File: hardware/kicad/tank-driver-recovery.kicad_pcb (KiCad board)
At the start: 2 copper layers, 170 x 110 mm, 15 parts, among them P101 JTR-PRI, P102 JTR-SEC, P103 JTR-PWR, Q101 BD139-16, Q102 BD140-16, Q103 BD139-16, Q104 BD140-16, U101 OPA1656IDR, U102 OPA1656IDR, U103 OPA1656IDR, U104 OPA1656IDR

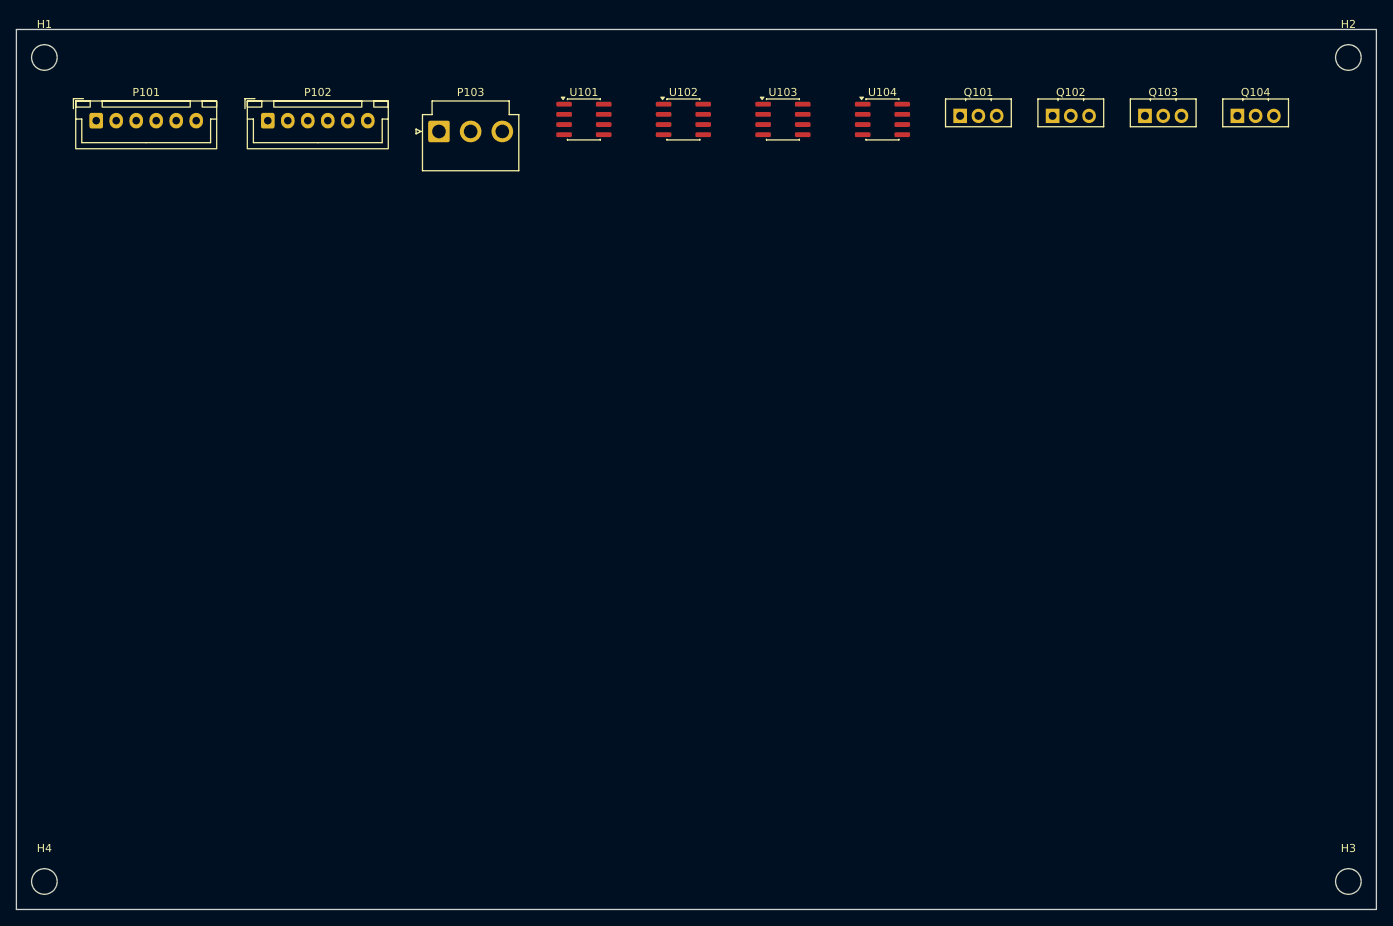
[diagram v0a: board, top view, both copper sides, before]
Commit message: Rev A: 3-pass schematic review + fixes, PCB sync + placement, parts freeze (2026-07-31)
Pass1+2 fixed cross-channel shorts (io rails/C1-C4/alias columns), ext-tank ghost wiring, U201 unit un-stack, U101-104 power units, PS500 pinout from datasheet, DRV renames. Decisions: TQ2-5V relays +D301, R241-3 deleted, PGND_IN+R502 link, K401-403 clip decoder, RCJ-041 tank jacks. GAS_Parts lib (TQ2/URA_YMD/RCJ-041), ~203 footprints, 6 boards synced+placed DRC-clean. Pass3 visual: paper sizes, stale notes. 3D GLBs + viewer. See hardware/kicad/schematic_review.md
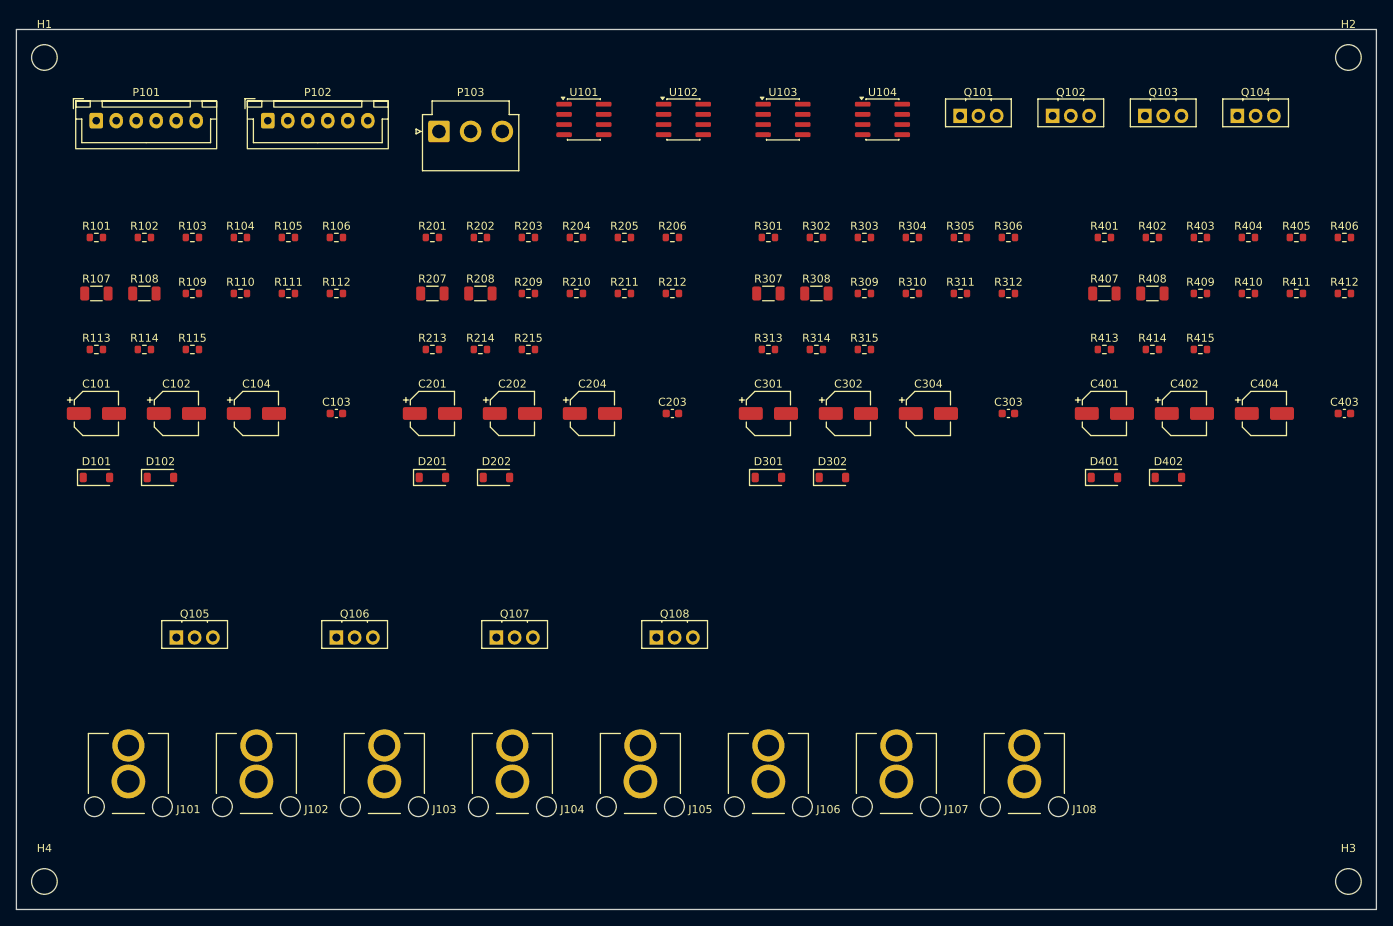
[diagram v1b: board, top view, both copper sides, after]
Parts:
- added C101: 10uF, Capacitor_SMD:CP_Elec_5x5.8, F.Cu at (10.0, 48.0)
- added C102: 10uF, Capacitor_SMD:CP_Elec_5x5.8, F.Cu at (20.0, 48.0)
- added C103: 220pF, Capacitor_SMD:C_0603_1608Metric, F.Cu at (40.0, 48.0)
- added C104: 10uF, Capacitor_SMD:CP_Elec_5x5.8, F.Cu at (30.0, 48.0)
- added C201: 10uF, Capacitor_SMD:CP_Elec_5x5.8, F.Cu at (52.0, 48.0)
- added C202: 10uF, Capacitor_SMD:CP_Elec_5x5.8, F.Cu at (62.0, 48.0)
- added C203: 220pF, Capacitor_SMD:C_0603_1608Metric, F.Cu at (82.0, 48.0)
- added C204: 10uF, Capacitor_SMD:CP_Elec_5x5.8, F.Cu at (72.0, 48.0)
- added C301: 10uF, Capacitor_SMD:CP_Elec_5x5.8, F.Cu at (94.0, 48.0)
- added C302: 10uF, Capacitor_SMD:CP_Elec_5x5.8, F.Cu at (104.0, 48.0)
- added C303: 220pF, Capacitor_SMD:C_0603_1608Metric, F.Cu at (124.0, 48.0)
- added C304: 10uF, Capacitor_SMD:CP_Elec_5x5.8, F.Cu at (114.0, 48.0)
- added C401: 10uF, Capacitor_SMD:CP_Elec_5x5.8, F.Cu at (136.0, 48.0)
- added C402: 10uF, Capacitor_SMD:CP_Elec_5x5.8, F.Cu at (146.0, 48.0)
- added C403: 220pF, Capacitor_SMD:C_0603_1608Metric, F.Cu at (166.0, 48.0)
- added C404: 10uF, Capacitor_SMD:CP_Elec_5x5.8, F.Cu at (156.0, 48.0)
- added D101: 1N4148, Diode_SMD:D_SOD-123, F.Cu at (10.0, 56.0)
- added D102: 1N4148, Diode_SMD:D_SOD-123, F.Cu at (18.0, 56.0)
- added D201: 1N4148, Diode_SMD:D_SOD-123, F.Cu at (52.0, 56.0)
- added D202: 1N4148, Diode_SMD:D_SOD-123, F.Cu at (60.0, 56.0)
- added D301: 1N4148, Diode_SMD:D_SOD-123, F.Cu at (94.0, 56.0)
- added D302: 1N4148, Diode_SMD:D_SOD-123, F.Cu at (102.0, 56.0)
- added D401: 1N4148, Diode_SMD:D_SOD-123, F.Cu at (136.0, 56.0)
- added D402: 1N4148, Diode_SMD:D_SOD-123, F.Cu at (144.0, 56.0)
- added J101: Primary L send, GAS_Parts:Jack_RCA_SameSky_RCJ-041_Horizontal, F.Cu at (14.0, 94.0)
- added J102: Primary L return, GAS_Parts:Jack_RCA_SameSky_RCJ-041_Horizontal, F.Cu at (30.0, 94.0)
- added J103: Primary R send, GAS_Parts:Jack_RCA_SameSky_RCJ-041_Horizontal, F.Cu at (46.0, 94.0)
- added J104: Primary R return, GAS_Parts:Jack_RCA_SameSky_RCJ-041_Horizontal, F.Cu at (62.0, 94.0)
- added J105: Secondary L send, GAS_Parts:Jack_RCA_SameSky_RCJ-041_Horizontal, F.Cu at (78.0, 94.0)
- added J106: Secondary L return, GAS_Parts:Jack_RCA_SameSky_RCJ-041_Horizontal, F.Cu at (94.0, 94.0)
- added J107: Secondary R send, GAS_Parts:Jack_RCA_SameSky_RCJ-041_Horizontal, F.Cu at (110.0, 94.0)
- added J108: Secondary R return, GAS_Parts:Jack_RCA_SameSky_RCJ-041_Horizontal, F.Cu at (126.0, 94.0)
- added Q105: BD139-16, Package_TO_SOT_THT:TO-126-3_Vertical, F.Cu at (20.0, 76.0)
- added Q106: BD140-16, Package_TO_SOT_THT:TO-126-3_Vertical, F.Cu at (40.0, 76.0)
- added Q107: BD139-16, Package_TO_SOT_THT:TO-126-3_Vertical, F.Cu at (60.0, 76.0)
- added Q108: BD140-16, Package_TO_SOT_THT:TO-126-3_Vertical, F.Cu at (80.0, 76.0)
- added R101: 10k, Resistor_SMD:R_0603_1608Metric, F.Cu at (10.0, 26.0)
- added R102: 100R, Resistor_SMD:R_0603_1608Metric, F.Cu at (16.0, 26.0)
- added R103: 2.2k, Resistor_SMD:R_0603_1608Metric, F.Cu at (22.0, 26.0)
- added R104: 2.2k, Resistor_SMD:R_0603_1608Metric, F.Cu at (28.0, 26.0)
- added R105: 100R, Resistor_SMD:R_0603_1608Metric, F.Cu at (34.0, 26.0)
- added R106: 100R, Resistor_SMD:R_0603_1608Metric, F.Cu at (40.0, 26.0)
- added R107: 10R, Resistor_SMD:R_1206_3216Metric, F.Cu at (10.0, 33.0)
- added R108: 10R, Resistor_SMD:R_1206_3216Metric, F.Cu at (16.0, 33.0)
- added R109: 1k, Resistor_SMD:R_0603_1608Metric, F.Cu at (22.0, 33.0)
- added R110: 47R, Resistor_SMD:R_0603_1608Metric, F.Cu at (28.0, 33.0)
- added R111: 100k, Resistor_SMD:R_0603_1608Metric, F.Cu at (34.0, 33.0)
- added R112: 2.2k, Resistor_SMD:R_0603_1608Metric, F.Cu at (40.0, 33.0)
- added R113: 1k, Resistor_SMD:R_0603_1608Metric, F.Cu at (10.0, 40.0)
- added R114: 47k, Resistor_SMD:R_0603_1608Metric, F.Cu at (16.0, 40.0)
- added R115: 100k, Resistor_SMD:R_0603_1608Metric, F.Cu at (22.0, 40.0)
- added R201: 10k, Resistor_SMD:R_0603_1608Metric, F.Cu at (52.0, 26.0)
- added R202: 100R, Resistor_SMD:R_0603_1608Metric, F.Cu at (58.0, 26.0)
- added R203: 2.2k, Resistor_SMD:R_0603_1608Metric, F.Cu at (64.0, 26.0)
- added R204: 2.2k, Resistor_SMD:R_0603_1608Metric, F.Cu at (70.0, 26.0)
- added R205: 100R, Resistor_SMD:R_0603_1608Metric, F.Cu at (76.0, 26.0)
- added R206: 100R, Resistor_SMD:R_0603_1608Metric, F.Cu at (82.0, 26.0)
- added R207: 10R, Resistor_SMD:R_1206_3216Metric, F.Cu at (52.0, 33.0)
- added R208: 10R, Resistor_SMD:R_1206_3216Metric, F.Cu at (58.0, 33.0)
- added R209: 1k, Resistor_SMD:R_0603_1608Metric, F.Cu at (64.0, 33.0)
- added R210: 47R, Resistor_SMD:R_0603_1608Metric, F.Cu at (70.0, 33.0)
- added R211: 100k, Resistor_SMD:R_0603_1608Metric, F.Cu at (76.0, 33.0)
- added R212: 2.2k, Resistor_SMD:R_0603_1608Metric, F.Cu at (82.0, 33.0)
- added R213: 1k, Resistor_SMD:R_0603_1608Metric, F.Cu at (52.0, 40.0)
- added R214: 47k, Resistor_SMD:R_0603_1608Metric, F.Cu at (58.0, 40.0)
- added R215: 100k, Resistor_SMD:R_0603_1608Metric, F.Cu at (64.0, 40.0)
- added R301: 10k, Resistor_SMD:R_0603_1608Metric, F.Cu at (94.0, 26.0)
- added R302: 100R, Resistor_SMD:R_0603_1608Metric, F.Cu at (100.0, 26.0)
- added R303: 2.2k, Resistor_SMD:R_0603_1608Metric, F.Cu at (106.0, 26.0)
- added R304: 2.2k, Resistor_SMD:R_0603_1608Metric, F.Cu at (112.0, 26.0)
- added R305: 100R, Resistor_SMD:R_0603_1608Metric, F.Cu at (118.0, 26.0)
- added R306: 100R, Resistor_SMD:R_0603_1608Metric, F.Cu at (124.0, 26.0)
- added R307: 10R, Resistor_SMD:R_1206_3216Metric, F.Cu at (94.0, 33.0)
- added R308: 10R, Resistor_SMD:R_1206_3216Metric, F.Cu at (100.0, 33.0)
- added R309: 1k, Resistor_SMD:R_0603_1608Metric, F.Cu at (106.0, 33.0)
- added R310: 47R, Resistor_SMD:R_0603_1608Metric, F.Cu at (112.0, 33.0)
- added R311: 100k, Resistor_SMD:R_0603_1608Metric, F.Cu at (118.0, 33.0)
- added R312: 2.2k, Resistor_SMD:R_0603_1608Metric, F.Cu at (124.0, 33.0)
- added R313: 1k, Resistor_SMD:R_0603_1608Metric, F.Cu at (94.0, 40.0)
- added R314: 47k, Resistor_SMD:R_0603_1608Metric, F.Cu at (100.0, 40.0)
- added R315: 100k, Resistor_SMD:R_0603_1608Metric, F.Cu at (106.0, 40.0)
- added R401: 10k, Resistor_SMD:R_0603_1608Metric, F.Cu at (136.0, 26.0)
- added R402: 100R, Resistor_SMD:R_0603_1608Metric, F.Cu at (142.0, 26.0)
- added R403: 2.2k, Resistor_SMD:R_0603_1608Metric, F.Cu at (148.0, 26.0)
- added R404: 2.2k, Resistor_SMD:R_0603_1608Metric, F.Cu at (154.0, 26.0)
- added R405: 100R, Resistor_SMD:R_0603_1608Metric, F.Cu at (160.0, 26.0)
- added R406: 100R, Resistor_SMD:R_0603_1608Metric, F.Cu at (166.0, 26.0)
- added R407: 10R, Resistor_SMD:R_1206_3216Metric, F.Cu at (136.0, 33.0)
- added R408: 10R, Resistor_SMD:R_1206_3216Metric, F.Cu at (142.0, 33.0)
- added R409: 1k, Resistor_SMD:R_0603_1608Metric, F.Cu at (148.0, 33.0)
- added R410: 47R, Resistor_SMD:R_0603_1608Metric, F.Cu at (154.0, 33.0)
- added R411: 100k, Resistor_SMD:R_0603_1608Metric, F.Cu at (160.0, 33.0)
- added R412: 2.2k, Resistor_SMD:R_0603_1608Metric, F.Cu at (166.0, 33.0)
- added R413: 1k, Resistor_SMD:R_0603_1608Metric, F.Cu at (136.0, 40.0)
- added R414: 47k, Resistor_SMD:R_0603_1608Metric, F.Cu at (142.0, 40.0)
- added R415: 100k, Resistor_SMD:R_0603_1608Metric, F.Cu at (148.0, 40.0)
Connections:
- P101 pad 1: (no net) -> PRI_RET_R
- P101 pad 2: (no net) -> PRI_SEND_R
- P101 pad 3: (no net) -> AGND
- P101 pad 4: (no net) -> PRI_RET_L
- P101 pad 5: (no net) -> PRI_SEND_L
- P101 pad 6: (no net) -> AGND
- P102 pad 1: (no net) -> SEC_RET_R
- P102 pad 2: (no net) -> SEC_SEND_R
- P102 pad 3: (no net) -> AGND
- P102 pad 4: (no net) -> SEC_RET_L
- P102 pad 5: (no net) -> SEC_SEND_L
- P102 pad 6: (no net) -> AGND
- P103 pad 1: (no net) -> +15VA
- P103 pad 2: (no net) -> AGND
- P103 pad 3: (no net) -> PWR_FLAG
- Q101 pad 1: (no net) -> PL_Q101_E
- Q101 pad 2: (no net) -> +15VA
- Q101 pad 3: (no net) -> PL_Q101_B
- Q102 pad 1: (no net) -> PL_Q102_E
- Q102 pad 2: (no net) -> -15VA
- Q102 pad 3: (no net) -> PL_Q102_B
- Q103 pad 1: (no net) -> PR_Q103_E
- Q103 pad 2: (no net) -> +15VA
- Q103 pad 3: (no net) -> PR_Q103_B
- Q104 pad 1: (no net) -> PR_Q104_E
- Q104 pad 2: (no net) -> -15VA
- Q104 pad 3: (no net) -> PR_Q104_B
- U101 pad 1: (no net) -> PL_DRV_OUT
- U101 pad 2: (no net) -> PL_DRV_FB
- U101 pad 3: (no net) -> PL_DRV_IN
- U101 pad 4: (no net) -> -15VA
- U101 pad 5: (no net) -> PL_REC_IN
- U101 pad 6: (no net) -> PL_REC_FB
- U101 pad 7: (no net) -> PL_REC_OUT
- U101 pad 8: (no net) -> +15VA
- U102 pad 1: (no net) -> PR_DRV_OUT
- U102 pad 2: (no net) -> PR_DRV_FB
- U102 pad 3: (no net) -> PR_DRV_IN
- U102 pad 4: (no net) -> -15VA
- U102 pad 5: (no net) -> PR_REC_IN
- U102 pad 6: (no net) -> PR_REC_FB
- U102 pad 7: (no net) -> PR_REC_OUT
- U102 pad 8: (no net) -> +15VA
- U103 pad 1: (no net) -> SL_DRV_OUT
- U103 pad 2: (no net) -> SL_DRV_FB
- U103 pad 3: (no net) -> SL_DRV_IN
- U103 pad 4: (no net) -> -15VA
- U103 pad 5: (no net) -> SL_REC_IN
- U103 pad 6: (no net) -> SL_REC_FB
- U103 pad 7: (no net) -> SL_REC_OUT
- U103 pad 8: (no net) -> +15VA
- U104 pad 1: (no net) -> SR_DRV_OUT
- U104 pad 2: (no net) -> SR_DRV_FB
- U104 pad 3: (no net) -> SR_DRV_IN
- U104 pad 4: (no net) -> -15VA
- U104 pad 5: (no net) -> SR_REC_IN
- U104 pad 6: (no net) -> SR_REC_FB
- U104 pad 7: (no net) -> SR_REC_OUT
- U104 pad 8: (no net) -> +15VA
